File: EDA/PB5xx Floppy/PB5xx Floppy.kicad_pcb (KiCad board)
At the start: 2 copper layers, 20 x 60 mm, 4 parts, among them J1 PowerBook, J2 IDC20

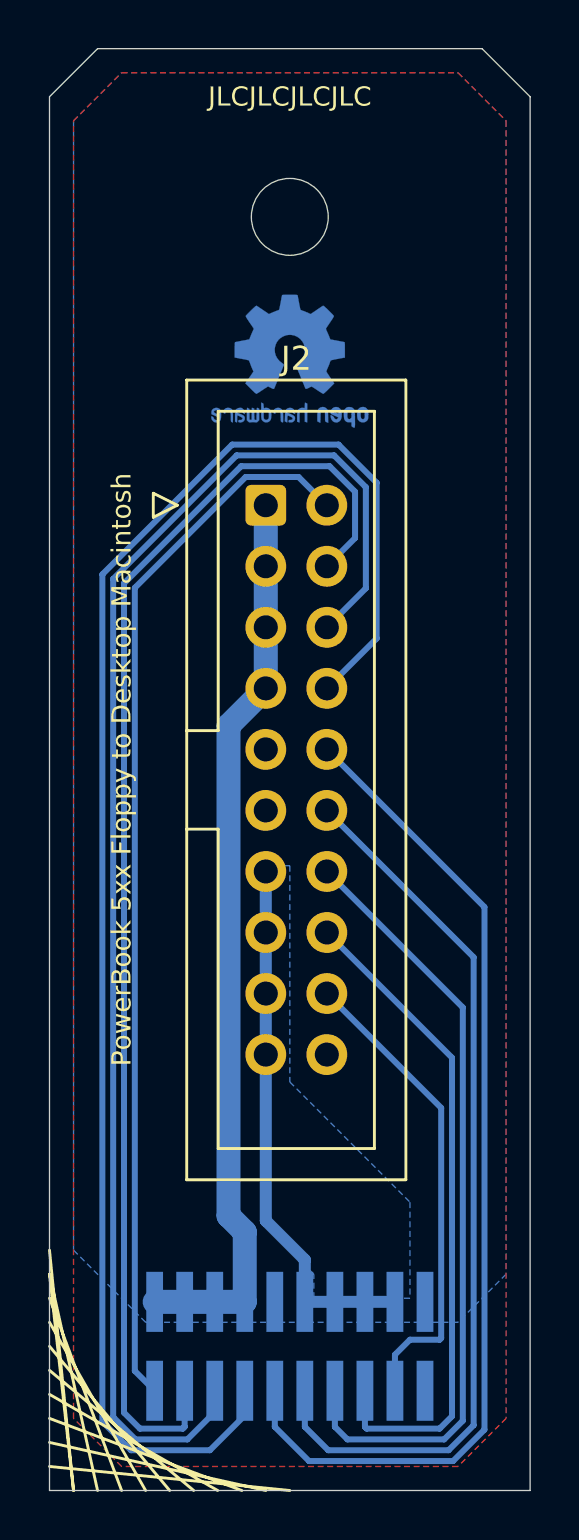
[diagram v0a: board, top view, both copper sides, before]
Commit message: PB5xx Floppy adapter V.1.1: changed connector + power LED
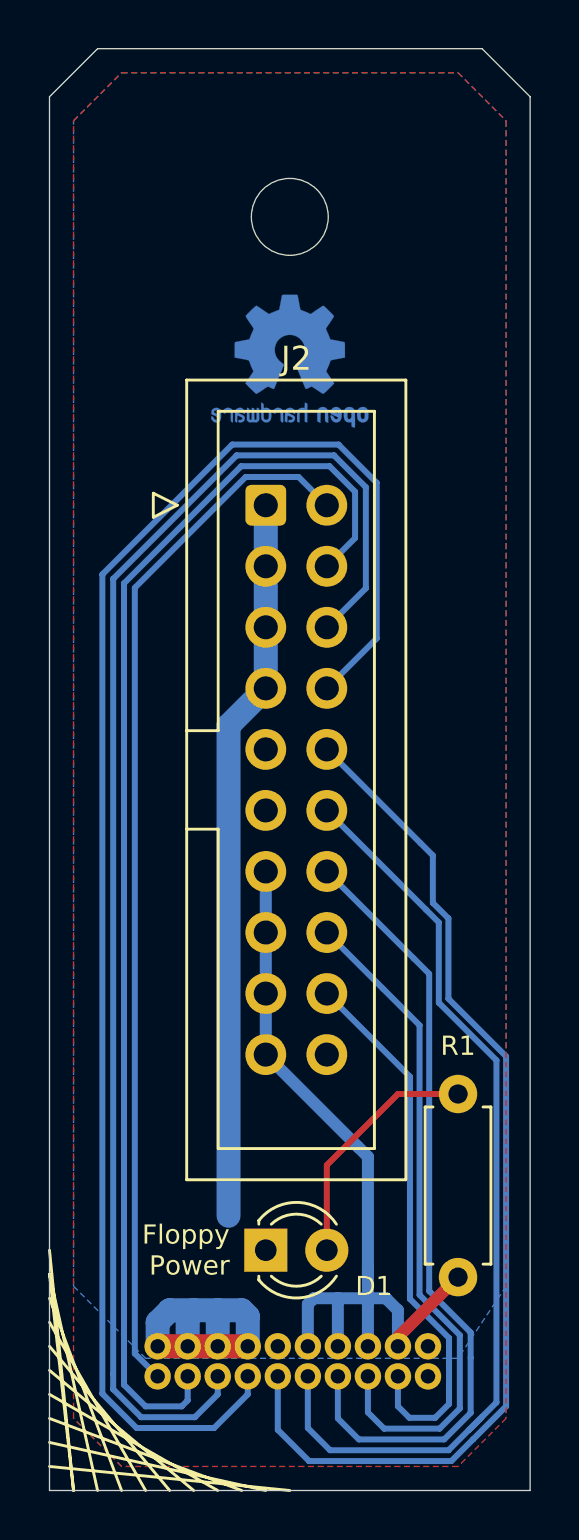
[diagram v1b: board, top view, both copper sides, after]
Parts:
- added D1: LED, LED_THT:LED_D3.0mm, F.Cu at (49.0, 160.0)
- added R1: 300, Resistor_THT:R_Axial_DIN0207_L6.3mm_D2.5mm_P7.62mm_Horizontal, F.Cu at (57.0, 153.5)
- J1: footprint G125-MS12005L0P:G125-MS11005L0P -> G125-MV12005L0P:G125-MV12005L0P
- moved J1 5.50 mm to (44.5, 164.0)
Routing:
- net +5V: track 22.3 -> 35.4 mm
- net Net-(D1-Pad2): track 0.00 -> 10.2 mm
- net GND: track 37.8 -> 43.4 mm
- net /WR: track 20.0 -> 23.0 mm
- net /SEL: track 37.5 -> 39.5 mm
- net /PH1: track 54.5 -> 53.1 mm
- net /~WREQ: track 42.4 -> 43.6 mm
- net /PH3: track 67.0 -> 65.8 mm
- net /PH2: track 60.5 -> 59.4 mm
- net /PH0: track 44.1 -> 43.6 mm
- net /~ENABLE: track 32.6 -> 33.1 mm
- removed copper zone on B.Cu, net +5V
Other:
- net class +VCC: clearance 0.2 -> 0.15
- net class Default: clearance 0.2 -> 0.15
- net class GND: clearance 0.2 -> 0.15
- rule trace_clearance: 0.2 -> 0.15
- board text added: "Floppy Power"
